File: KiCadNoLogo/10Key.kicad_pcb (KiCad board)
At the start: 2 copper layers, 73 x 102.5 mm, 57 parts, among them P1 USB_OTG, P2 Program, Q1 MMBT3906, Q2 MMBT3906, Q3 MMBT3906, Q4 MMBT3906, Q5 MMBT3906, SW1 SW_PUSH, SW10 5, SW11 2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

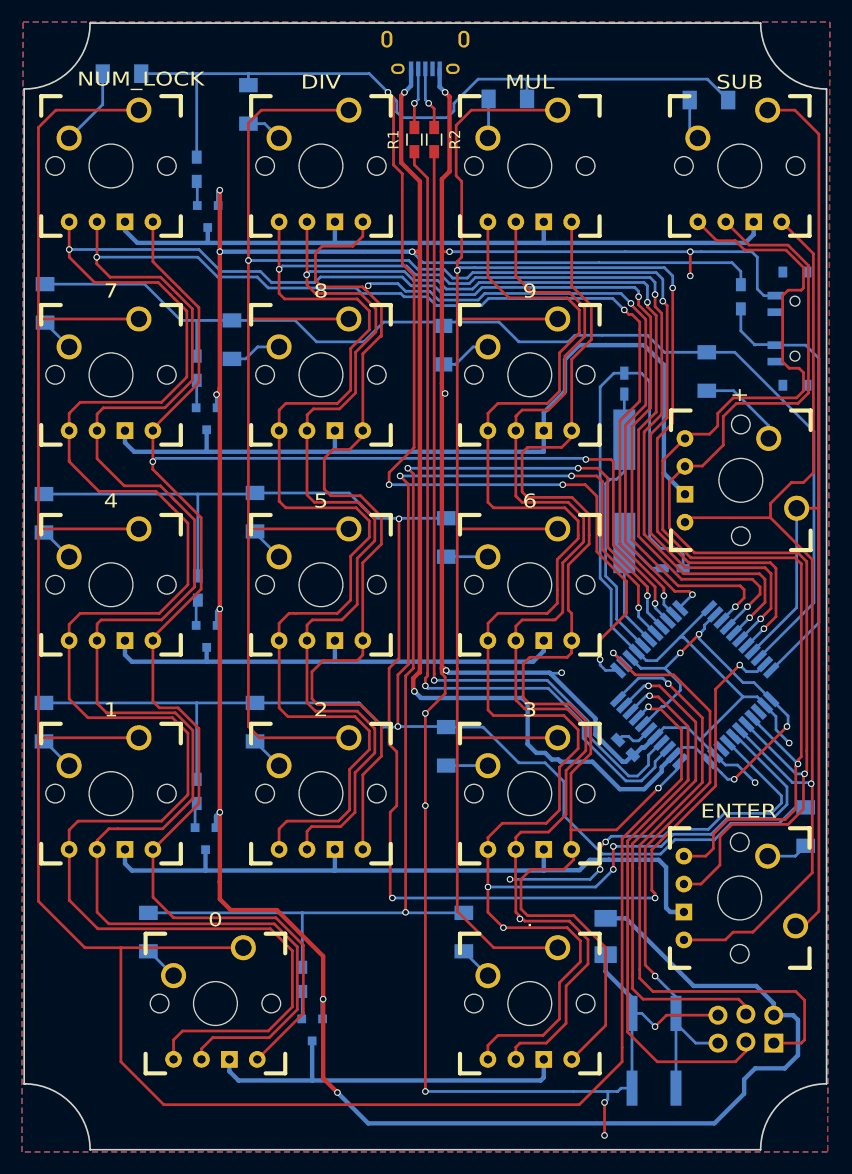
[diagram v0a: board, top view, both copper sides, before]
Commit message: Updated no logo pcb with current limiting resistors.
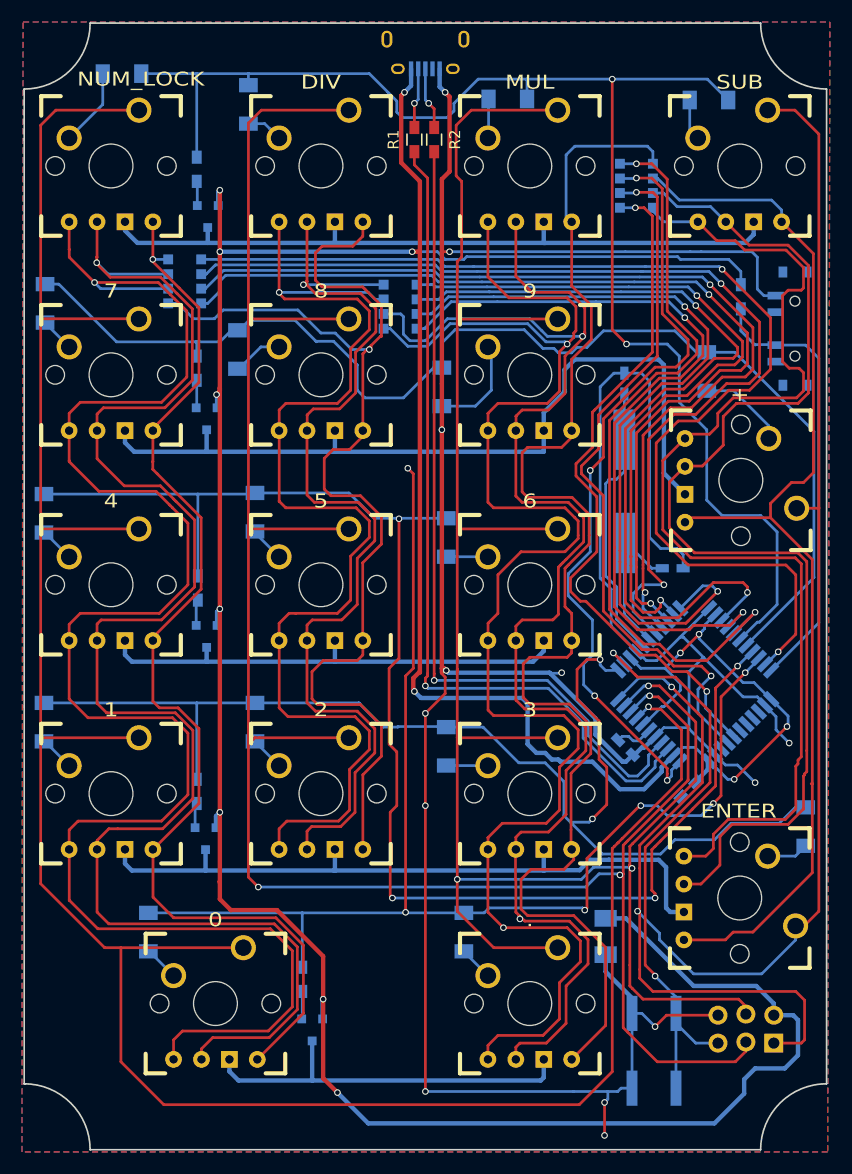
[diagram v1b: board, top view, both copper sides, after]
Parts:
- added C5: 0.1uF, Capacitors_SMD:C_0603_HandSoldering, B.Cu at (170.9, 118.2)
- added RP1: 100, Resistors_SMD:R_Array_Convex_4x1206, B.Cu at (125.1, 72.0)
- added RP2: 100, Resistors_SMD:R_Array_Convex_4x1206, B.Cu at (144.7, 74.3)
- added RP3: 100, Resistors_SMD:R_Array_Convex_4x1206, B.Cu at (166.2, 63.3)
- moved D11 3.80 mm to (148.5, 81.6)
- moved D7 1.03 mm to (129.9, 78.2)
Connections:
- P2 pad 1: /MISO -> /COL3
- P2 pad 3: /SCK -> /COL1
- P2 pad 4: /MOSI -> /COL2
- U1 pad 1: /LEDR2 -> Net-(RP3-Pad3)
- U1 pad 10: /MOSI -> /COL2
- U1 pad 11: /MISO -> /COL3
- U1 pad 12: /ROW0 -> /ROW3
- U1 pad 18: /ROW3 -> Net-(RP1-Pad2)
- U1 pad 19: /ROW4 -> Net-(RP1-Pad3)
- U1 pad 20: /LEDR0 -> Net-(RP1-Pad4)
- U1 pad 21: /LEDG0 -> Net-(RP2-Pad1)
- U1 pad 22: /LEDR1 -> Net-(RP2-Pad3)
- U1 pad 25: /LEDB0 -> Net-(RP2-Pad2)
- U1 pad 26: /LEDG1 -> Net-(RP2-Pad4)
- U1 pad 27: /LEDB1 -> Net-(RP3-Pad4)
- U1 pad 28: /COL1 -> /ROW0
- U1 pad 29: /COL2 -> /ROW1
- U1 pad 30: /COL3 -> /ROW2
- U1 pad 31: /ROW1 -> /ROW4
- U1 pad 32: /ROW2 -> Net-(RP1-Pad1)
- U1 pad 37: /LEDB3 -> Net-(U1-Pad37)
- U1 pad 38: /LEDG3 -> Net-(U1-Pad38)
- U1 pad 39: /LEDR3 -> Net-(U1-Pad39)
- U1 pad 40: /LEDB2 -> Net-(RP3-Pad1)
- U1 pad 41: /LEDG2 -> Net-(RP3-Pad2)
- U1 pad 9: /SCK -> /COL1
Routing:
- net Net-(RP1-Pad1): track 0.00 -> 103.7 mm, vias 0 -> 2
- net Net-(RP1-Pad2): track 0.00 -> 92.0 mm, vias 0 -> 2
- net Net-(RP1-Pad4): track 0.00 -> 87.7 mm, vias 0 -> 2
- net Net-(RP1-Pad3): track 0.00 -> 87.7 mm, vias 0 -> 2
- net /LEDB0: track 247.5 -> 160.5 mm, vias 3 -> 1
- net Net-(RP2-Pad2): track 0.00 -> 78.3 mm, vias 0 -> 2
- net /LEDG0: track 220.5 -> 145.6 mm, vias 3 -> 1
- net Net-(RP2-Pad3): track 0.00 -> 73.2 mm, vias 0 -> 2
- net Net-(RP2-Pad4): track 0.00 -> 72.7 mm, vias 0 -> 2
- net Net-(RP3-Pad3): track 0.00 -> 71.8 mm, vias 0 -> 4
- net Net-(RP3-Pad4): track 0.00 -> 69.3 mm, vias 0 -> 2
- net /LEDB1: track 174.8 -> 106.6 mm, vias 3 -> 1
- net Net-(RP2-Pad1): track 0.00 -> 67.5 mm, vias 0 -> 2
- net /LEDG1: track 157.8 -> 91.8 mm, vias 3 -> 1
- net Net-(RP3-Pad2): track 0.00 -> 65.0 mm, vias 0 -> 2
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
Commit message: Added current limiting resistors.
A bunch of clean up.  Added current limiting resistors.  Moved a number of connections off of the JTAG pins so that they don't need to have fuses reconfigured.
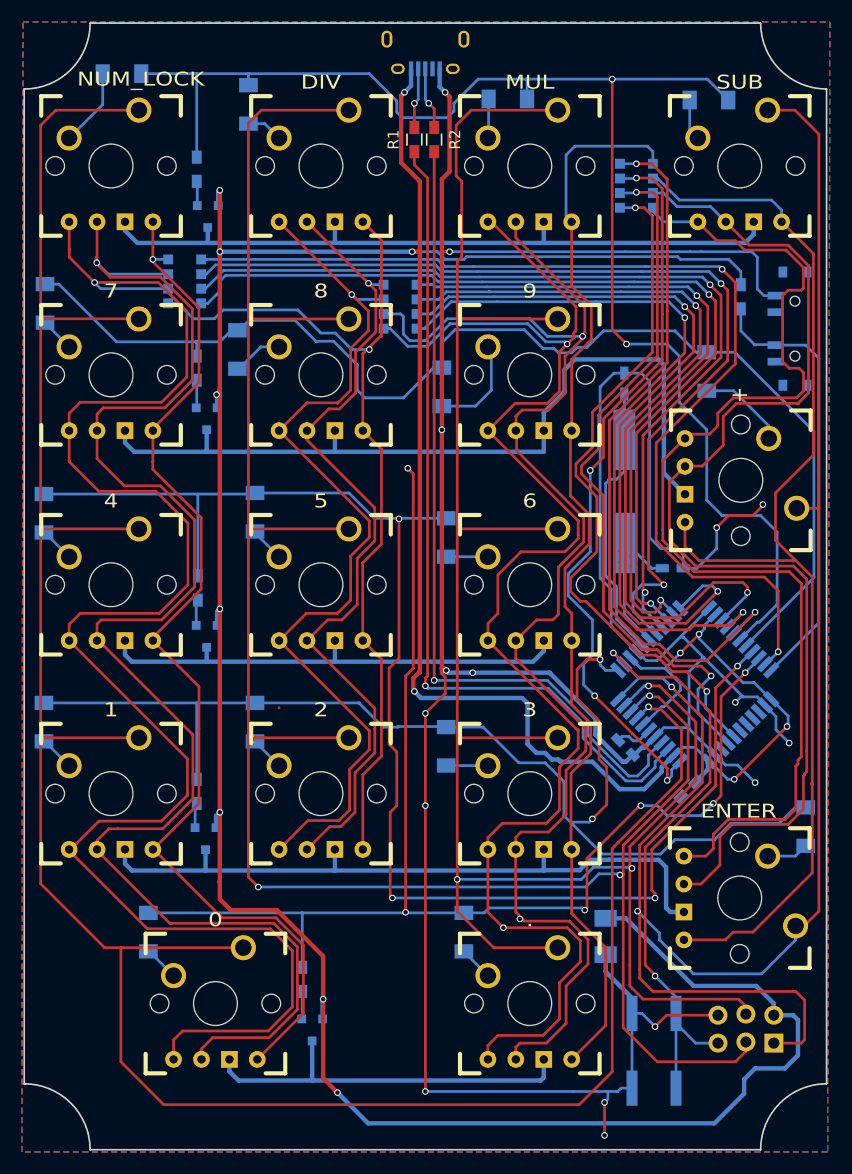
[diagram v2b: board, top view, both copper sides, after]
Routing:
- net /LEDR2: track 123.3 -> 100.4 mm
- net /LEDB1: track 106.6 -> 85.7 mm
- net /LEDR1: track 103.4 -> 83.2 mm
- net /LEDG1: track 91.8 -> 75.9 mm
- net /LEDB2: track 146.2 -> 134.8 mm
- net GND: track 291.9 -> 302.6 mm, vias 13 -> 16
- net /LEDB0: track 160.5 -> 152.4 mm
- net Net-(RP1-Pad1): track 103.7 -> 96.2 mm
- net /LEDG2: track 134.8 -> 127.4 mm
- net /LEDG0: track 145.6 -> 138.8 mm
- net Net-(RP2-Pad2): track 78.3 -> 73.5 mm
- net Net-(RP1-Pad2): track 92.0 -> 87.3 mm
- net Net-(RP1-Pad3): track 87.7 -> 82.9 mm
- net Net-(RP2-Pad1): track 67.5 -> 62.8 mm
- net Net-(RP1-Pad4): track 87.7 -> 83.1 mm
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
